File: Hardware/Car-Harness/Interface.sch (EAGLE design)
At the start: 56 parts, among them J1 34912-8020, J2 34912-8020, J4 632722110112, J5 OBDII-FEMALEFEMALE, Q1 6.5A/20V/35mΩ, Q2 5.8A/30V/35mΩ, Q3 6.5A/20V/35mΩ, Q4 5.8A/30V/35mΩ

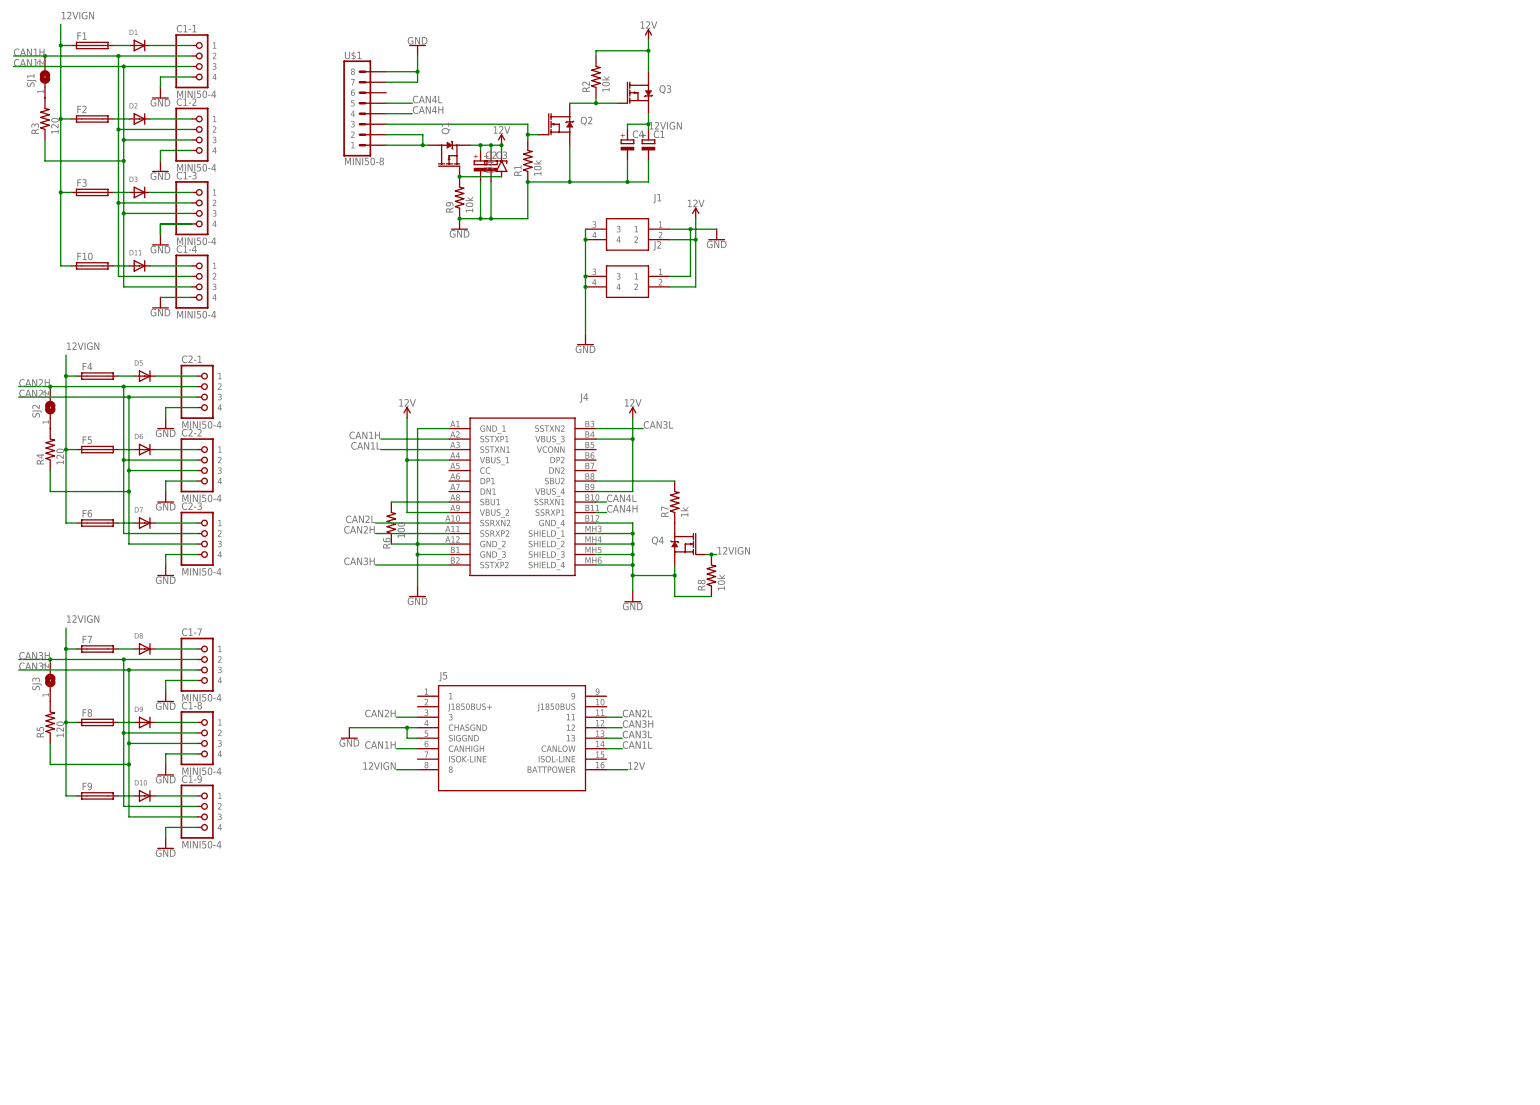
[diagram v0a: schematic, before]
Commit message: ibooster v2, stm32teensy work
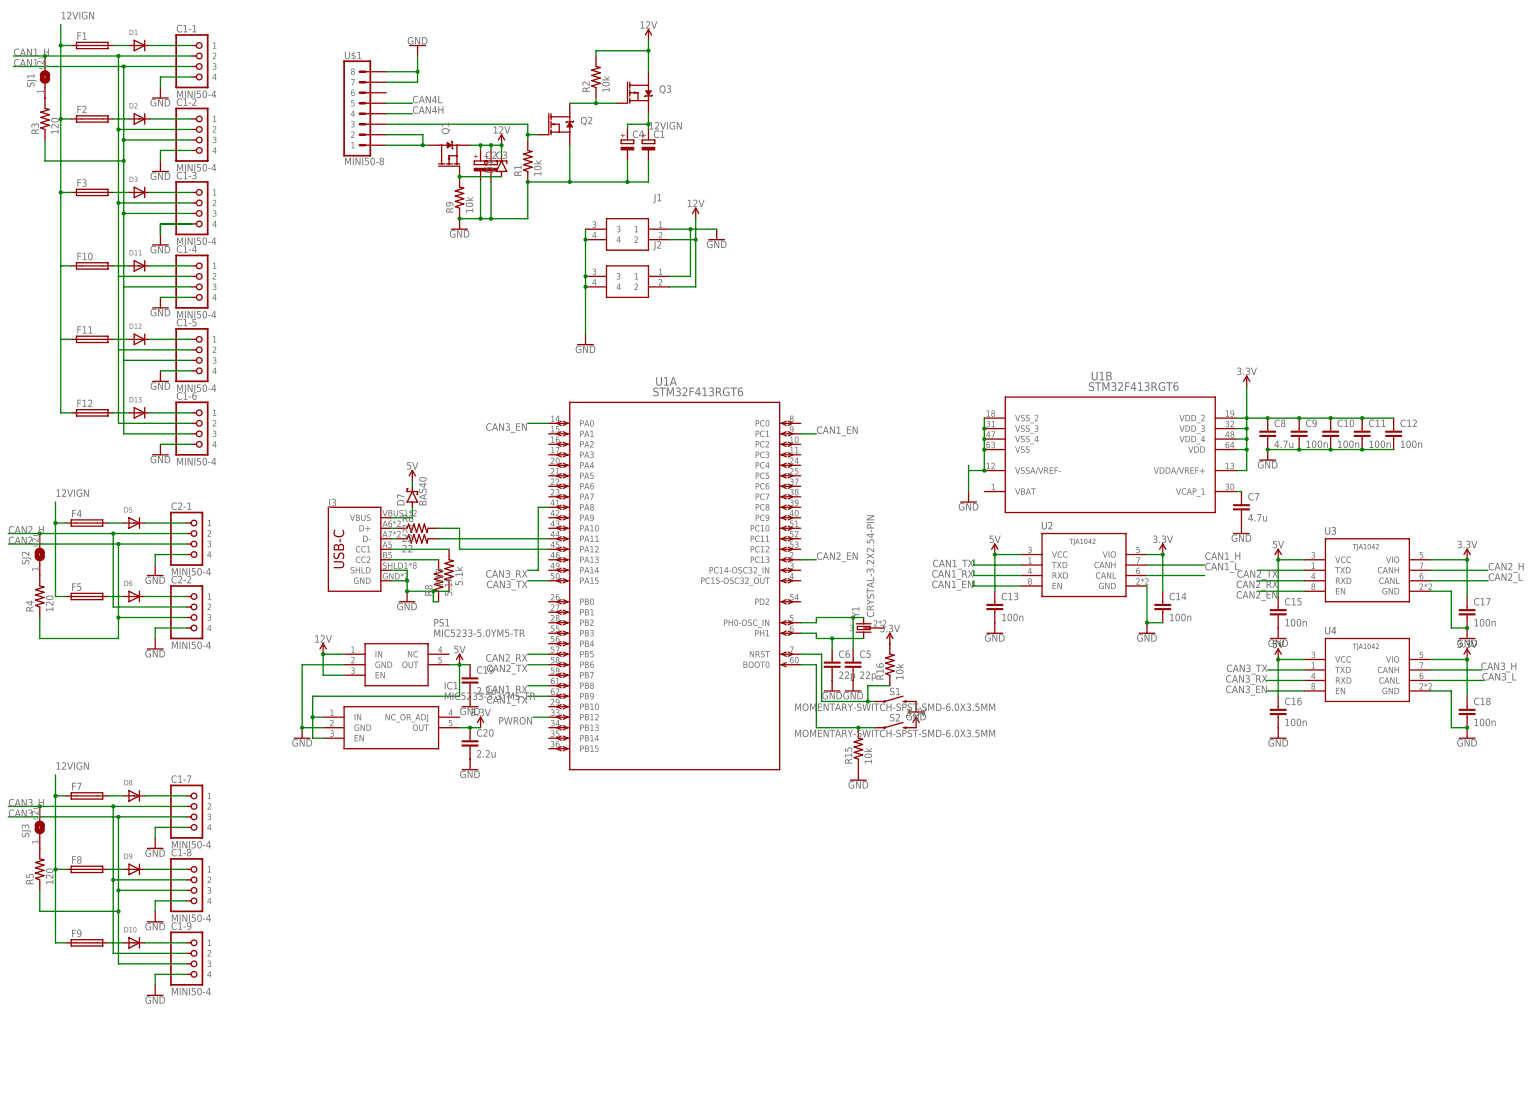
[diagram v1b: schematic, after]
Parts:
- removed C2-3: MINI50-4, interceptor:MINI50-4
- removed F6: FUSE_CHIP-1206(3216-METRIC), Circuit-Protection:FUSE_CHIP-1206(3216-METRIC)
- removed J4: 632722110112, SamacSys_Parts:632722110112
- removed J5: OBDII-FEMALEFEMALE, interceptor:OBDII-FEMALEFEMALE
- removed Q4: 5.8A/30V/35mΩ, SparkFun-DiscreteSemi:MOSFET-NCH-AO3404A
- added C1-5, C1-6: MINI50-4, interceptor:MINI50-4
- added C10, C11, C12, C13, C14, C15, C16, C17, C18, C9: 100n, comma.ai:C0603
- added C19, C20: 2.2u, comma.ai:C0603
- added C5, C6: 22p, comma.ai:C0603
- added C7, C8: 4.7u, comma.ai:C0603
- added D12, D13: (no value), adafruit:DIODESOD-323F
- added F11, F12: FUSE_CHIP-1206(3216-METRIC), Circuit-Protection:FUSE_CHIP-1206(3216-METRIC)
- added IC1: MIC5233-3.3YM5-TR, SamacSys_Parts:MIC5233-3.3YM5-TR
- added J3: (no value), ROTR-Wireless:USB-C-BREAKOUT_SPARKFUN-CONNECTORS_USB_C16PIN
- added PS1: MIC5233-5.0YM5-TR, SamacSys_Parts:MIC5233-5.0YM5-TR
- added R10: 5.1k, comma.ai:R0402
- added R15, R16: 10k, comma.ai:R0402
- added S1, S2: MOMENTARY-SWITCH-SPST-SMD-6.0X3.5MM, SparkFun-Switches:MOMENTARY-SWITCH-SPST-SMD-6.0X3.5MM
- added U1: STM32F413RGT6, interceptor:STM32F413RGT6
- added U2, U3, U4: TJA1042HVSON, comma.ai:TJA1042HVSON
- added Y1: CRYSTAL-3.2X2.54-PIN, comma.ai:CRYSTAL-3.2X2.54-PIN
- D7: value (none) -> BAS40; device adafruit:DIODESOD-323F -> diode:BAS40
- R6: value 100 -> 22; device interceptor:R0402 -> comma.ai:R0402
- R7: value 1k -> 22; device interceptor:R0402 -> comma.ai:R0402
- R8: value 10k -> 5.1k; device interceptor:R0402 -> comma.ai:R0402
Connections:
- removed net CAN1H: C1-1.2, C1-2.2, C1-3.2, C1-4.2, J4.SSTXP1, J5.CANHIGH, SJ1.2
- removed net CAN1L: C1-1.3, C1-2.3, C1-3.3, C1-4.3, J4.SSTXN1, J5.CANLOW, R3.1
- removed net CAN2H: C2-1.2, C2-2.2, C2-3.2, J4.SSRXP2, J5.3, SJ2.2
- removed net CAN2L: C2-1.3, C2-2.3, C2-3.3, J4.SSRXN2, J5.11, R4.1
- removed net CAN3H: C1-7.2, C1-8.2, C1-9.2, J4.SSTXP2, J5.12, SJ3.2
- removed net CAN3L: C1-7.3, C1-8.3, C1-9.3, J4.SSTXN2, J5.13, R5.1
- new net 12VIGN1: F11.1
- new net 12VIGN2: F12.1
- new net 3.3V: C10.1, C11.1, C12.1, C14.1, C17.1, C18.1, C20.1, C8.1, C9.1, IC1.OUT, R16.2, S2.2, U1B.VDD, U1B.VDDA/VREF+, U1B.VDD_2, U1B.VDD_3, U1B.VDD_4, U2.VIO, U3.VIO, U4.VIO
- new net 5V: C13.1, C15.1, C16.1, C19.1, D7.C, IC1.EN, IC1.IN, PS1.OUT, U2.VCC, U3.VCC, U4.VCC
- new net CAN1H1: C1-5.2
- new net CAN1H2: C1-6.2
- new net CAN1L1: C1-5.3
- new net CAN1L2: C1-6.3
- new net CAN1_EN: U1A.PC1, U2.EN
- new net CAN1_H: C1-1.2, C1-2.2, C1-3.2, C1-4.2, SJ1.2, U2.CANH
- new net CAN1_L: C1-1.3, C1-2.3, C1-3.3, C1-4.3, R3.1, U2.CANL
- new net CAN1_RX: U1A.PB8, U2.RXD
- new net CAN1_TX: U1A.PB9, U2.TXD
- new net CAN2_EN: U1A.PC13, U3.EN
- new net CAN2_H: C2-1.2, C2-2.2, SJ2.2, U3.CANH
- new net CAN2_L: C2-1.3, C2-2.3, R4.1, U3.CANL
- new net CAN2_RX: U1A.PB5, U3.RXD
- new net CAN2_TX: U1A.PB6, U3.TXD
- new net CAN3_EN: U1A.PA0, U4.EN
- new net CAN3_H: C1-7.2, C1-8.2, C1-9.2, SJ3.2, U4.CANH
- new net CAN3_L: C1-7.3, C1-8.3, C1-9.3, R5.1, U4.CANL
- new net CAN3_RX: U1A.PA8, U4.RXD
- new net CAN3_TX: U1A.PA15, U4.TXD
- new net N$31: C1-6.1, D13.C
- new net N$32: R6.2, U1A.PA12
- new net N$33: J3.CC1, R10.2
- new net N$34: J3.CC2, R8.2
- new net N$35: J3.D+, R6.1
- new net N$36: J3.D-, R7.1
- new net N$37: D7.A, J3.VBUS
- new net N$38: R16.1, S1.1, U1A.NRST
- new net N$39: R15.2, S2.1, U1A.BOOT0
- new net N$40: C7.1, U1B.VCAP_1
- new net N$43: C6.1, U1A.PH1, Y1.1
- new net PWRON: U1A.PB12
- net 12V: now also PS1.EN, PS1.IN; no longer J4.VBUS_1, J4.VBUS_2, J4.VBUS_3, J4.VBUS_4, J5.BATTPOWER
- net 12VIGN: no longer F6.1, J5.8, Q4.G, R8.2
- net CAN4H: no longer J4.SSRXP1
- net CAN4L: no longer J4.SSRXN1
- net GND: now also C1-5.4, C1-6.4, C10.2, C11.2, C12.2, C13.2, C14.2, C15.2, C16.2, C17.2, C18.2, C19.2, C20.2, C5.2, C6.2, C7.2, C8.2, C9.2, IC1.GND, J3.GND, J3.SHLD, PS1.GND, R10.1, R15.1, S1.2, U1B.VSS, U1B.VSSA/VREF-, U1B.VSS_2, U1B.VSS_3, U1B.VSS_4, U2.GND, U3.GND, U4.GND; no longer C2-3.4, J4.GND_1, J4.GND_2, J4.GND_3, J4.GND_4, J4.SHIELD_1, J4.SHIELD_2, J4.SHIELD_3, J4.SHIELD_4, J5.CHASGND, J5.SIGGND, Q4.S, R6.1
- net N$14: now also C5.1, U1A.PH0-OSC_IN, Y1.2; no longer D7.A, F6.2
- net N$16: now also R7.2, U1A.PA11; no longer C2-3.1, D7.C
- net N$25: now also D12.A, F11.2; no longer J4.SBU2, R7.2
- net N$29: now also C1-5.1, D12.C; no longer Q4.D, R7.1
- net N$30: now also D13.A, F12.2; no longer J4.SBU1, R6.2
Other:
- moved on the sheet: C1-7, C1-8, C1-9, C2-1, C2-2, D10, D5, D6, D8, D9, F4, F5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

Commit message: ibooster gateway
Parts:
- removed D7: BAS40, diode:BAS40
- removed R10, R8: 5.1k, comma.ai:R0402
- added U$2: TPS25830, packages(ti):TPS25830
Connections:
- removed net CAN4H: U$1.4
- removed net CAN4L: U$1.5
- new net N$41: J3.D-, U$2.DM_IN
- new net N$42: J3.VBUS, U$2.BUS
- new net N$44: J3.GND, J3.SHLD
- net 5V: no longer D7.C
- net GND: now also U$1.6; no longer J3.GND, J3.SHLD, R10.1, R8.1
- net N$10: now also U$1.3
- net N$12: now also U$1.5; no longer U$1.3
- net N$33: now also U$2.CC1; no longer R10.2
- net N$34: now also U$2.CC2; no longer R8.2
- net N$35: no longer J3.D+
- net N$36: no longer J3.D-
- net N$37: now also J3.D+, U$2.DP_IN; no longer D7.A, J3.VBUS
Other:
- moved on the sheet: J3

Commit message: some shit
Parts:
- removed J2: 34912-8020, SamacSys_Parts:34912-8020
- added C21, C25, C26, C27, C28: 10u, comma.ai:C0603
- added C22, C24, C29, C30, C34: 0.1u, comma.ai:C0603
- added C23: 2.2u, comma.ai:C0603
- added C31, C32, C35: 0.22u, comma.ai:C0603
- added C33: 1u, comma.ai:C0603
- added D7: (no value), adafruit:DIODESOD-323F
- added L1: SRP7028A-100M, SRP7028A-100M:SRP7028A-100M
- added LED1: CREE-RGB-CLVBA, comma.ai:CREE-RGB-CLVBA
- added Q4: PMOSFET, Transistor:PMOSFET_SOT23
- added Q5: 5.8A/30V/35mΩ, SparkFun-DiscreteSemi:MOSFET-NCH-AO3404A
- added R10, R11, R8: 120, interceptor:R0402
- added R12: 100, interceptor:R0402
- added R13: 300, interceptor:R0402
- added R14: 0.015, interceptor:R0402
- added R17: 50k, comma.ai:R0402
- added R18, R19, R22: 100k, comma.ai:R0402
- added R20: 12.8k, comma.ai:R0402
- added R21: 11.8k, comma.ai:R0402
- added R23: 10k, interceptor:R0402
- added U$3: MICROFIT-6, interceptor:MICROFIT-6
- U2, U3, U4: value TJA1042HVSON -> TJA1042; device comma.ai:TJA1042HVSON -> CM,118:TJA1042
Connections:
- removed net 12VIGN1: F11.1
- removed net 12VIGN2: F12.1
- removed net CAN1H1: C1-5.2
- removed net CAN1H2: C1-6.2
- removed net CAN1L1: C1-5.3
- removed net CAN1L2: C1-6.3
- new net B: R10.1, U1A.PC6
- new net CTL1: R18.1, U$2.CTRL1
- new net CTL2: R19.1, U$2.CTRL2, U1A.PA13
- new net D+: J3.D+, R6.1, U$2.DP_IN
- new net D-: J3.D-, R7.1, U$2.DM_IN
- new net EN: U$2.EN/UVLO, U1A.PB2
- new net G: R8.1, U1A.PC7
- new net GPSEN: Q4.G, R22.1, U1A.PC14-OSC32_IN
- new net GPSRST: U$3.4, U1A.PC5
- new net N$45: LED1.G-, R8.2
- new net N$46: LED1.R-, R11.1
- new net N$47: LED1.B-, R10.2
- new net N$49: Q4.D, U$3.1
- new net N$50: Q5.D, U1A.PA1
- new net N$52: C35.1, R12.2, U$2.BUS
- new net N$54: C23.1, C24.1, R18.2, R19.2, U$2.VCC
- new net N$56: C25.1, C26.1, C27.1, C28.1, C29.1, L1.2, R13.1, R14.2
- new net N$57: R13.2, U$2.CSP
- new net N$58: C34.2, U$2.BOOT
- new net N$59: R17.2, U$2.RT/SYNC
- new net R: R11.2, U1A.PC9
- new net UART_RX: U$3.6, U1A.PA10
- new net UART_TX: U$3.5, U1A.PA9
- net 12V: now also C21.1, C22.1, Q3.S, U$2.IN; no longer J2.2, Q3.D
- net 12VIGN: now also F11.1, F12.1, Q3.D, Q5.G, R23.2; no longer Q3.S
- net 3.3V: now also LED1.COM+, Q4.S, R22.2, U$3.2
- net 5V: now also D7.C
- net CAN1_H: now also C1-5.2, C1-6.2
- net CAN1_L: now also C1-5.3, C1-6.3
- net GND: now also C21.2, C22.2, C23.2, C24.2, C25.2, C26.2, C27.2, C28.2, C30.1, C31.2, C32.2, C33.1, C35.2, J3.GND, J3.SHLD, Q5.S, R17.1, R20.1, R21.1, R23.1, U$2.AGND, U$2.PGND, U$3.3; no longer J2.1, J2.3, J2.4
- net N$33: now also C31.1
- net N$34: now also C32.1
- net N$35: now also U1A.PC3; no longer R6.1
- net N$36: now also U1A.PC2; no longer R7.1
- net N$37: now also R20.2, U$2.IMON; no longer J3.D+, U$2.DP_IN
- net N$41: now also R21.2, U$2.ILIM; no longer J3.D-, U$2.DM_IN
- net N$42: now also C29.2, C30.2, C33.2, D7.A, R12.1, R14.1, U$2.CSN/OUT; no longer U$2.BUS
- net N$44: now also C34.1, L1.1, U$2.SW; no longer J3.GND, J3.SHLD
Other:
- moved on the sheet: Q3, R6, U2, U3, U4
